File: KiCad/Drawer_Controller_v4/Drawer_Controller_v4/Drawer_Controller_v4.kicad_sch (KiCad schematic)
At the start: 21 parts, among them J1 Conn_02x04_Odd_Even, J2 Conn_02x03_Odd_Even, J4 Conn_02x05_Odd_Even, U3 PESD2CANFD24L-TR, X12 Conn_01x03_2.5mm_JST_S04B-XAS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, X13 Conn_01x08_2.5mm_JST_S04B-XAS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, X14 Conn_01x02_2.5mm_JST_S02B-XAS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, X3 Conn_01x04_2.5mm_JST_S04B-XAS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, X4 Conn_02x03_3.0mm_Molex_Micro_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, X5 RJ45_45_degree_angled

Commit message: feat: placed all parts for `Drawer_Controller_v4` and routed about 80%
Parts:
- removed H3, H4: MountingHole, Robast:MountingHole_3.2mm_M3_Pad_Top_6.4mm_Bottom_9.4mm, symbol Mechanical:MountingHole
- added H5, H6: MountingHole, MountingHole:MountingHole_2.2mm_M2_DIN965_Pad_TopBottom, symbol Mechanical:MountingHole
- H1, H2: footprint Robast:MountingHole_3.2mm_M3_Pad_Top_6.4mm_Bottom_9.4mm -> Robast:MountingHole_3.2mm_M3_Pad_Top_Bottom_9.2mm
- H3: renamed from H5; footprint Robast:MountingHole_3.2mm_M3_Pad_Top_6.4mm_Bottom_9.4mm -> Robast:MountingHole_3.2mm_M3_Pad_Top_Bottom_9.2mm
- H4: renamed from H6; footprint Robast:MountingHole_3.2mm_M3_Pad_Top_6.4mm_Bottom_9.4mm -> Robast:MountingHole_3.2mm_M3_Pad_Top_Bottom_9.2mm
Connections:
- net Drawer_1_OA1: now also X3.2 (Pin_2); no longer X3.3 (Pin_3)
- net Drawer_1_OA2: now also X3.1 (Pin_1); no longer X3.4 (Pin_4)
- net Drawer_1_OB1: now also X3.3 (Pin_3); no longer X3.1 (Pin_1)
- net Drawer_1_OB2: now also X3.4 (Pin_4); no longer X3.2 (Pin_2)
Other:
- note added: "M2 for cable ties"
- moved on the sheet: H3, H4

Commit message: feat: completed `Drawer_Controller_v4`
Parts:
- renumbered C64 to C1, F2 to F1, F1 to F2, J4 to J1, J1 to J3, R231 to R1, R235 to R2, U3 to U1, X5 to X1, X14 to X2, X13 to X3, X12 to X5, X3 to X6
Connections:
- net pe_2_IO0_0 renamed pe_0_IO0_3
- net pe_2_IO0_3 renamed pe_0_IO0_4
- net pe_2_IO0_4 renamed pe_0_IO0_5
- net pe_2_IO1_1 renamed pe_0_IO0_7
- net pe_2_IO1_6 renamed pe_0_IO0_6

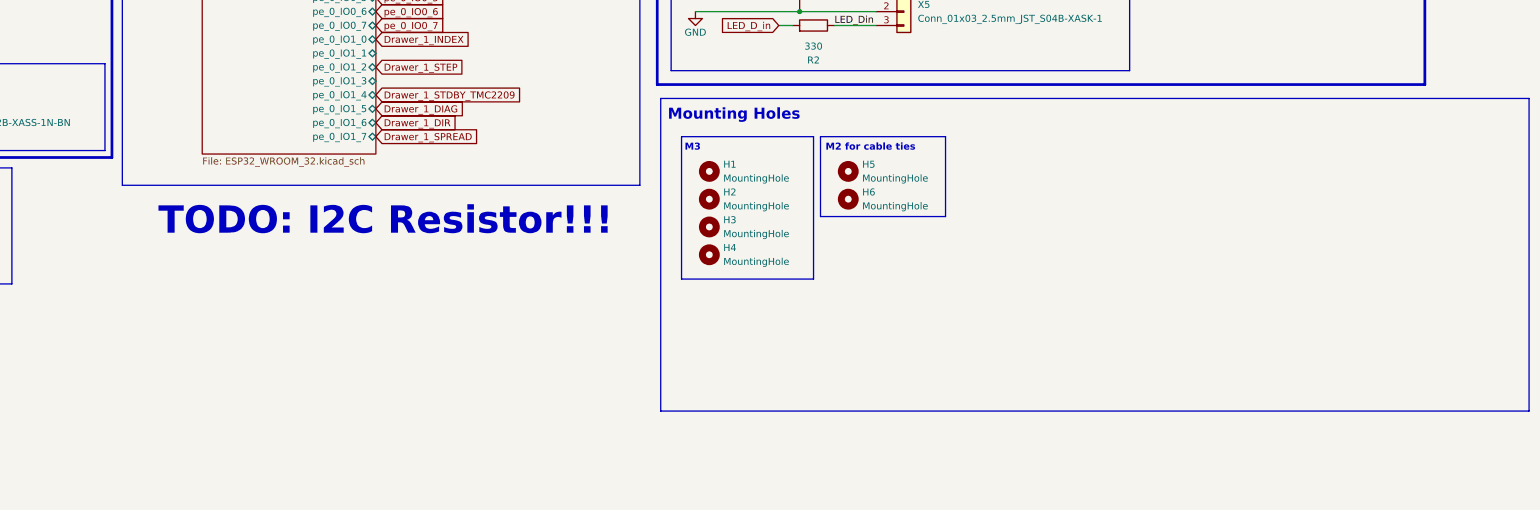
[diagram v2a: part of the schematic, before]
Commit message: feat: small final changes and creation of manufacturing files for `Drawer_Controller_v4`
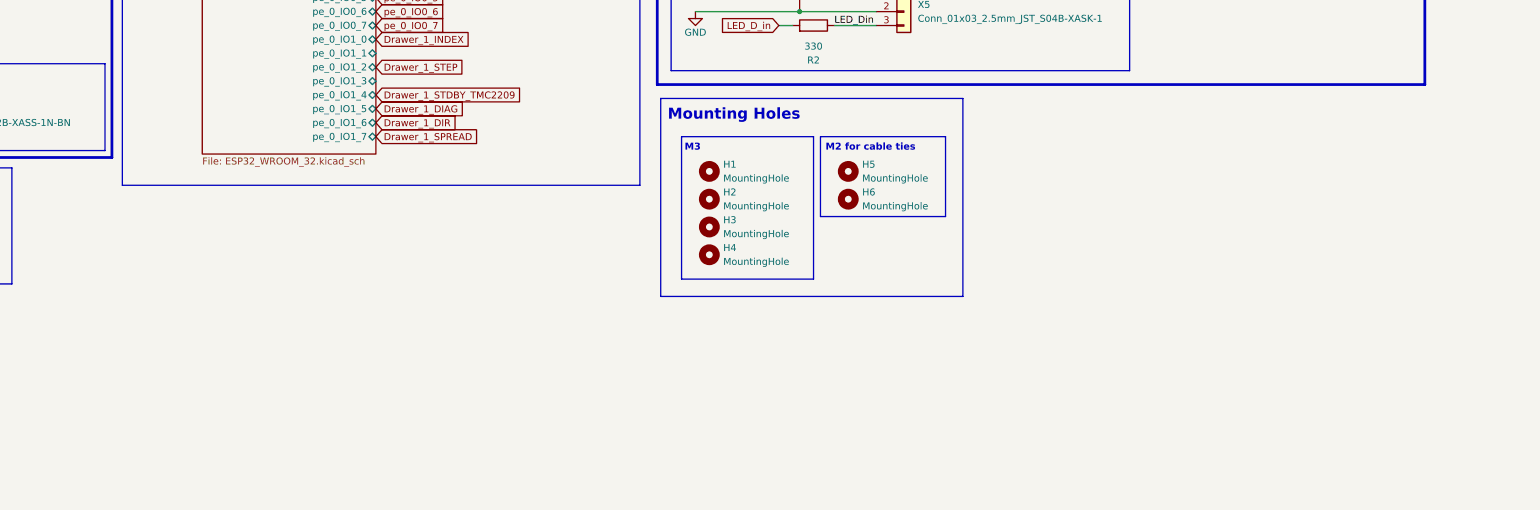
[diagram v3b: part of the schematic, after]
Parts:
- X1, X4: now left out of the parts list
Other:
- note removed: "TODO: I2C Resistor!!!"
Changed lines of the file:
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@@
 	(rectangle
 		(start 246.38 120.015)
-		(end 405.13 177.165)
+		(end 301.625 156.21)
 		(stroke
 			(width 0)
@@
 		)
 	)
-	(text "TODO: I2C Resistor!!!"
-		(exclude_from_sim no)
-		(at 196.088 142.494 0)
-		(effects
-			(font
-				(size 5 5)
-				(thickness 1)
-				(bold yes)
-				(color 255 0 0 1)
-			)
-		)
-	)
 	(text "Mounting Holes"
 		(exclude_from_sim no)
@@
 		(unit 1)
 		(exclude_from_sim no)
-		(in_bom yes)
+		(in_bom no)
 		(on_board yes)
 		(dnp no)
@@
 		(unit 1)
 		(exclude_from_sim no)
-		(in_bom yes)
+		(in_bom no)
 		(on_board yes)
 		(dnp no)

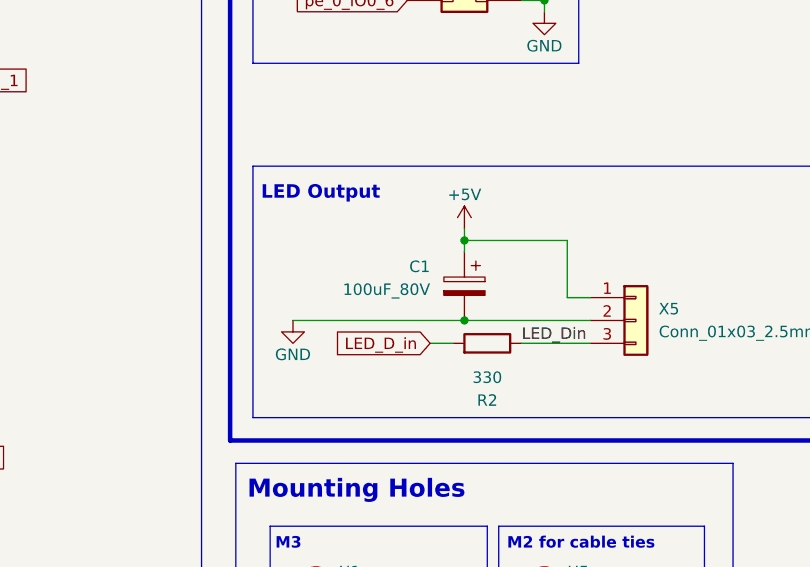
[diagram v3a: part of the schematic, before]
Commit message: feat: replaces `CP_Elec_12.5x13.5` with `CP_Elec_10x10`
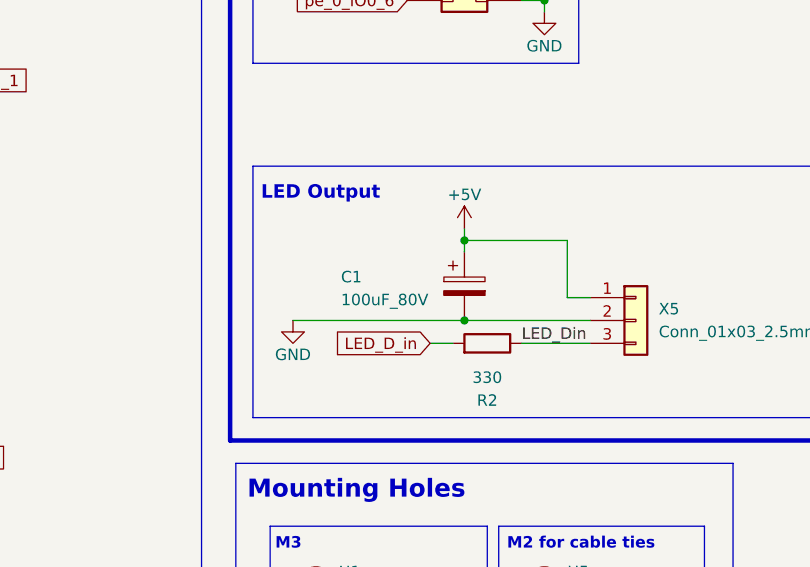
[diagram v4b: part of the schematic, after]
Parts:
- C1: footprint Robast:CP_Elec_12.5x13.5 -> Capacitor_SMD:CP_Elec_10x10; MPN VZH101M1KTR-1313 -> VZH101M1KTR-1010; OC_LCSC C249839 -> C249838; OC_MOUSER (none) -> 140-VZH101M1KTR1010
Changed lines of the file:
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@@
 	)
 	(junction
+		(at 271.78 104.14)
+		(diameter 0)
+		(color 0 0 0 0)
+	)
+	(junction
 		(at 59.69 80.01)
 		(diameter 0)
@@
 	)
 	(junction
-		(at 271.78 104.14)
-		(diameter 0)
-		(color 0 0 0 0)
-	)
-	(junction
 		(at 278.13 36.83)
 		(diameter 0)
@@
 	(wire
 		(pts
+			(xy 271.78 104.14) (xy 285.75 104.14)
+		)
+		(stroke
+			(width 0)
+			(type default)
+		)
+	)
+	(wire
+		(pts
 			(xy 38.1 101.6) (xy 41.91 101.6)
 		)
@@
 	(wire
 		(pts
-			(xy 271.78 104.14) (xy 285.75 104.14)
+			(xy 252.73 104.14) (xy 271.78 104.14)
 		)
 		(stroke
@@
 	(wire
 		(pts
-			(xy 252.73 104.14) (xy 271.78 104.14)
-		)
-		(stroke
-			(width 0)
-			(type default)
-		)
-	)
-	(wire
-		(pts
 			(xy 214.63 45.72) (xy 214.63 49.53)
 		)
@@
 	)
 	(symbol
-		(lib_id "_C_Polarized:100uF_80V")
-		(at 271.78 100.33 0)
-		(mirror y)
-		(unit 1)
-		(exclude_from_sim no)
-		(in_bom yes)
-		(on_board yes)
-		(dnp no)
-		(property "Reference" "C1"
-			(at 267.97 98.1709 0)
-			(effects
-				(font
-					(size 1.27 1.27)
-				)
-				(justify left)
-			)
-		)
-		(property "Value" "100uF_80V"
-			(at 267.97 100.7109 0)
-			(effects
-				(font
-					(size 1.27 1.27)
-				)
-				(justify left)
-			)
-		)
-		(property "Footprint" "Robast:CP_Elec_12.5x13.5"
-			(at 270.8148 104.14 0)
-			(effects
-				(font
-					(size 1.27 1.27)
-				)
-				(hide yes)
-			)
-		)
-		(property "Datasheet" "https://www.mouser.de/datasheet/2/231/161587245243-2307006.pdf"
-			(at 271.78 100.33 0)
-			(effects
-				(font
-					(size 1.27 1.27)
-				)
-				(hide yes)
-			)
-		)
-		(property "Description" "Aluminum Electrolytic Capacitor 100uF 80V ±20% SMD,D12.5xL13.5mm"
-			(at 271.78 100.33 0)
-			(effects
-				(font
-					(size 1.27 1.27)
-				)
-				(hide yes)
-			)
-		)
-		(property "MF" "Lelon"
-			(at 271.78 100.33 0)
-			(effects
-				(font
-					(size 1.27 1.27)
-				)
-				(hide yes)
-			)
-		)
-		(property "MPN" "VZH101M1KTR-1313"
-			(at 271.78 100.33 0)
-			(effects
-				(font
-					(size 1.27 1.27)
-				)
-				(hide yes)
-			)
-		)
-		(property "OC_CONRAD" ""
-			(at 271.78 100.33 0)
-			(effects
-				(font
-					(size 1.27 1.27)
-				)
-				(hide yes)
-			)
-		)
-		(property "OC_LCSC" "C249839"
-			(at 271.78 100.33 0)
-			(effects
-				(font
-					(size 1.27 1.27)
-				)
-				(hide yes)
-			)
-		)
-		(property "OC_MOUSER" ""
-			(at 271.78 100.33 0)
-			(effects
-				(font
-					(size 1.27 1.27)
-				)
-				(hide yes)
-			)
-		)
-		(property "OC_RS" ""
-			(at 271.78 100.33 0)
-			(effects
-				(font
-					(size 1.27 1.27)
-				)
-				(hide yes)
-			)
-		)
-		(pin "1"
-		)
-		(pin "2"
-		)
-		(instances
-			(project "Drawer_Controller_v4"
-				(path "/57f8c193-fe09-43d3-9441-dbd40881d2aa"
-					(reference "C1")
-					(unit 1)
-				)
-			)
-		)
-	)
-	(symbol
 		(lib_id "_Connector_JST:Conn_01x02_2.5mm_JST_S02B-XASS-1N-BN")
 		(at 97.79 121.92 0)
@@
 					(unit 1)
 				)
+			)
+		)
+	)
+	(symbol
+		(lib_id "_C_Polarized:100uF_80V")
+		(at 271.78 100.33 0)
+		(unit 1)
+		(exclude_from_sim no)
+		(in_bom yes)
+		(on_board yes)
+		(dnp no)
+		(property "Reference" "C1"
+			(at 258.064 99.314 0)
+			(effects
+				(font
+					(size 1.27 1.27)
+				)
+				(justify left)
+			)
+		)
+		(property "Value" "100uF_80V"
+			(at 258.064 101.854 0)
+			(effects
+				(font
+					(size 1.27 1.27)
+				)
+				(justify left)
+			)
+		)
+		(property "Footprint" "Capacitor_SMD:CP_Elec_10x10"
+			(at 272.7452 104.14 0)
+			(effects
+				(font
+					(size 1.27 1.27)
+				)
+				(hide yes)
+			)
+		)
+		(property "Datasheet" "https://www.mouser.de/datasheet/2/231/161587245243-2307006.pdf"
+			(at 271.78 100.33 0)
+			(effects
+				(font
+					(size 1.27 1.27)
+				)
+				(hide yes)
+			)
+		)
+		(property "Description" "Aluminum Electrolytic Capacitor 100uF 80V ±20% SMD,D10xL10mm"
+			(at 271.78 100.33 0)
+			(effects
+				(font
+					(size 1.27 1.27)
+				)
+				(hide yes)
+			)
+		)
+		(property "MF" "Lelon"
+			(at 271.78 100.33 0)
+			(effects
+				(font
+					(size 1.27 1.27)
+				)
+				(hide yes)
+			)
+		)
+		(property "MPN" "VZH101M1KTR-1010"
+			(at 271.78 100.33 0)
+			(effects
+				(font
+					(size 1.27 1.27)
+				)
+				(hide yes)
+			)
+		)
+		(property "OC_CONRAD" ""
+			(at 271.78 100.33 0)
+			(effects
+				(font
+					(size 1.27 1.27)
+				)
+				(hide yes)
+			)
+		)
+		(property "OC_LCSC" "C249838"
+			(at 271.78 100.33 0)
+			(effects
+				(font
+					(size 1.27 1.27)
+				)
+				(hide yes)
+			)
+		)
+		(property "OC_MOUSER" "140-VZH101M1KTR1010 "
+			(at 271.78 100.33 0)
+			(effects
+				(font
+					(size 1.27 1.27)
+				)
+				(hide yes)
+			)
+		)
+		(property "OC_RS" ""
+			(at 271.78 100.33 0)
+			(effects
+				(font
+					(size 1.27 1.27)
+				)
+				(hide yes)
+			)
+		)
+		(pin "1"
+		)
+		(pin "2"
+		)
+		(instances
+			(project "Drawer_Controller_v4"
+				(path "/57f8c193-fe09-43d3-9441-dbd40881d2aa"
+					(reference "C1")
+					(unit 1)
+				)
